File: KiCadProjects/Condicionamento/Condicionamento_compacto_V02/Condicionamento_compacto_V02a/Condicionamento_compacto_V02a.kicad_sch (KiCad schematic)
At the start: 28 parts, among them J2 Canais, J3 Entrada, J6 In_1 select, J7 In_2 select, U1-buffer1 AD828AN, U2-gain1 AD828AN, U3-Cond-DIP1 AD828AN, U4-Cond-SMD1 AD8056ARZ, U4-DigPot2 X9c10x, U5-DigPot1 X9c10x, U5-buffer1 AD8056ARZ, U6-gain1 AD8056ARZ

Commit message: agc
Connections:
- net GND is gone; now on net Earth: J3.6 (Pin_6), U4-DigPot2.2 (GND), U4-DigPot2.6 (GND), U5-DigPot1.2 (GND), U5-DigPot1.6 (GND)
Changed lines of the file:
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@@
+    (stroke (width 0) (type default))
+  )
+  (wire (pts (xy 234.95 148.59) (xy 238.76 148.59))
     (stroke (width 0) (type default))
   )
@@
         (path "/ca05a78d-0094-4531-91c3-e609c3923191"
           (reference "C4") (unit 1)
+        )
+      )
+    )
+  )
+  (symbol (lib_id "power:GND") (at 238.76 148.59 0) (mirror y) (unit 1)
+    (in_bom yes) (on_board yes) (dnp no) (fields_autoplaced)
+    (property "Reference" "#PWR028" (at 238.76 154.94 0)
+      (effects (font (size 1.27 1.27)) hide)
+    )
+    (property "Value" "Earth" (at 238.76 152.4 0)
+      (effects (font (size 1.27 1.27)) hide)
+    )
+    (property "Footprint" "" (at 238.76 148.59 0)
+      (effects (font (size 1.27 1.27)) hide)
+    )
+    (property "Datasheet" "~" (at 238.76 148.59 0)
+      (effects (font (size 1.27 1.27)) hide)
+    )
+    (pin "1")
+    (instances
+      (project "Condicionamento_compacto_V02a"
+        (path "/ca05a78d-0094-4531-91c3-e609c3923191"
+          (reference "#PWR028") (unit 1)
         )
       )
@@
         )
       )
+    )
+  )
+  (symbol (lib_id "power:Earth") (at 234.95 148.59 0) (mirror y) (unit 1)
+    (in_bom yes) (on_board yes) (dnp no) (fields_autoplaced)
+    (property "Reference" "#PWR027" (at 234.95 154.94 0)
+      (effects (font (size 1.27 1.27)) hide)
+    )
+    (property "Value" "Earth" (at 234.95 152.4 0)
+      (effects (font (size 1.27 1.27)) hide)
+    )
+    (property "Footprint" "" (at 234.95 148.59 0)
+      (effects (font (size 1.27 1.27)) hide)
+    )
+    (property "Datasheet" "~" (at 234.95 148.59 0)
+      (effects (font (size 1.27 1.27)) hide)
+    )
+    (pin "1")
+    (instances
+      (project "Condicionamento_compacto_V02a"
+        (path "/ca05a78d-0094-4531-91c3-e609c3923191"
+          (reference "#PWR027") (unit 1)
+        )
+      )

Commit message: tmp
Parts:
- added Cf1, Cf2: C, symbol Device:C
- added J1: jumper cf1, symbol Connector_Generic:Conn_01x02
- added J4: jumper cf2, symbol Connector_Generic:Conn_01x02
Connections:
- net Earth: now also Cf1.2, Cf2.2
- net auxiliar_1: now also J1.2 (Pin_2)
- net auxiliar_2: now also J4.2 (Pin_2)
- new net: Cf1.1, J1.1 (Pin_1)
- new net: Cf2.1, J4.1 (Pin_1)
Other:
- moved on the sheet: J6, J7, R10, R11, U2-gain1, U4-DigPot2, U5-DigPot1

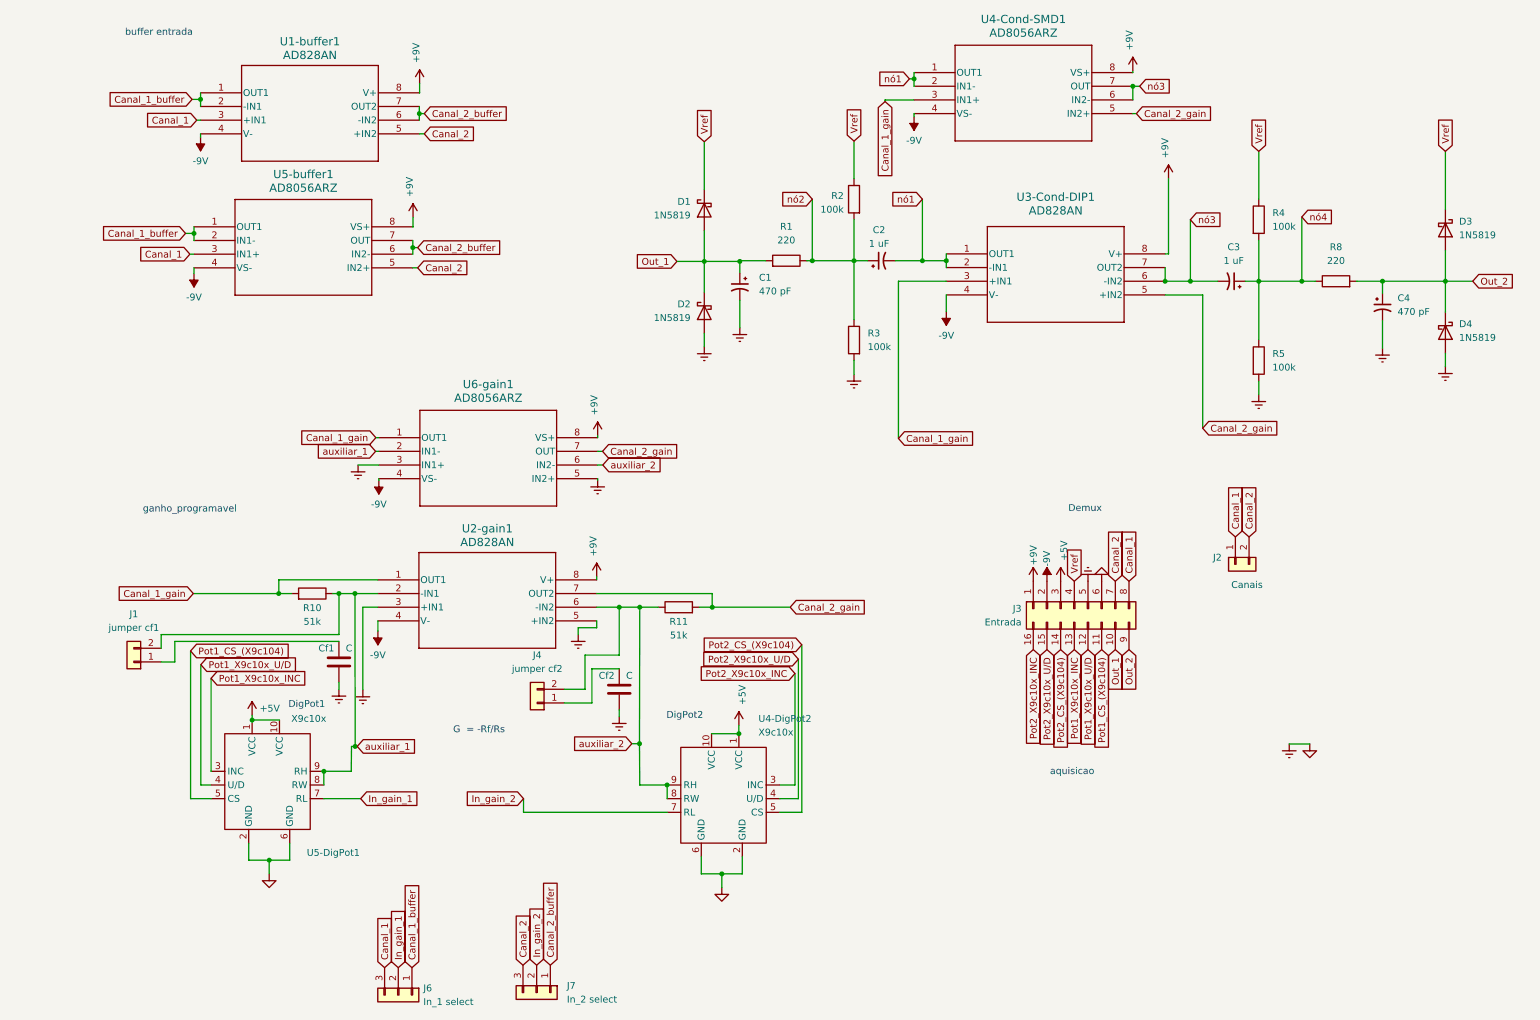
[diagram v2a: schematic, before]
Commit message: biblioteca analise sinal pelo osciloscopio
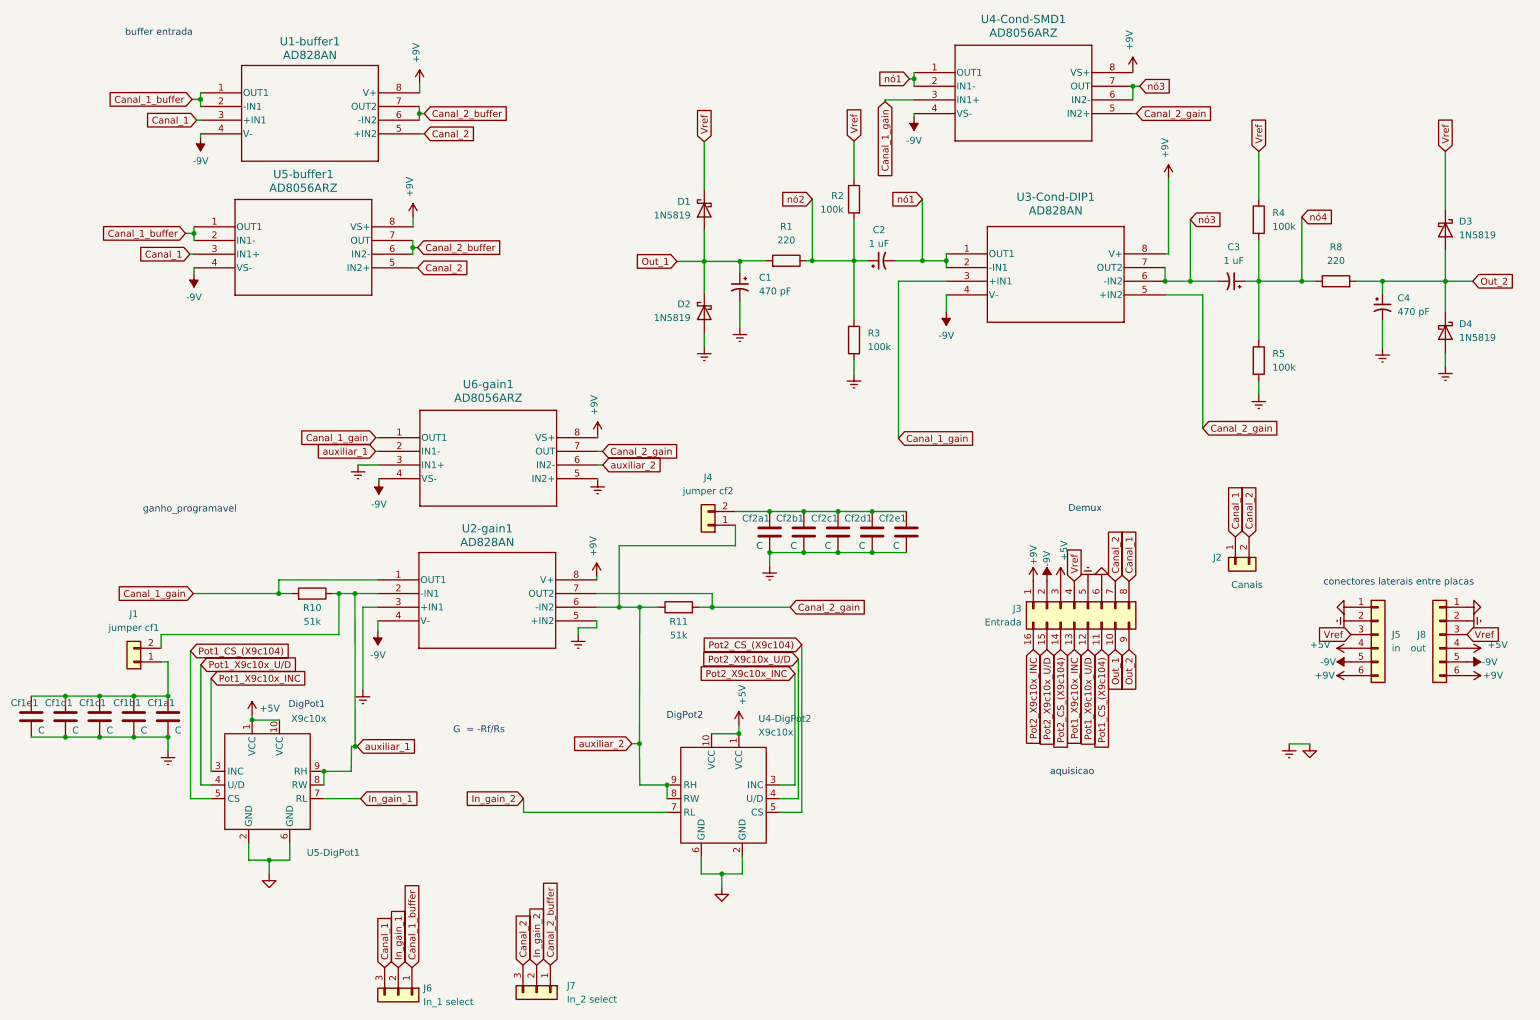
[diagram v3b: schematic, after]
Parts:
- removed Cf2: C, symbol Device:C
- added Cf1b1, Cf1c1, Cf1d1, Cf1e1, Cf2a1, Cf2b1, Cf2c1, Cf2d1, Cf2e1: C, Capacitor_THT:CP_Radial_D5.0mm_P2.50mm, symbol Device:C
- added J5: in, Connector_PinSocket_2.54mm:PinSocket_1x06_P2.54mm_Horizontal, symbol Connector_Generic:Conn_01x06
- added J8: out, Connector_PinHeader_2.54mm:PinHeader_1x06_P2.54mm_Horizontal, symbol Connector_Generic:Conn_01x06
- Cf1a1: renamed from Cf1; footprint (none) -> Capacitor_THT:CP_Radial_D5.0mm_P2.50mm
- J1: footprint (none) -> Connector_PinHeader_2.54mm:PinHeader_1x02_P2.54mm_Vertical
- J4: footprint (none) -> Connector_PinHeader_2.54mm:PinHeader_1x06_P2.54mm_Horizontal
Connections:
- net +5V: now also J5.4 (Pin_4), J8.4 (Pin_4)
- net +9V: now also J5.6 (Pin_6), J8.6 (Pin_6)
- net -9V: now also J5.5 (Pin_5), J8.5 (Pin_5)
- net Earth: now also Cf1b1.2, Cf1c1.2, Cf1d1.2, Cf1e1.2, Cf2a1.2, Cf2b1.2, Cf2c1.2, Cf2d1.2, Cf2e1.2, J5.1 (Pin_1), J5.2 (Pin_2), J8.1 (Pin_1), J8.2 (Pin_2)
- net Vref: now also J5.3 (Pin_3), J8.3 (Pin_3)
- net auxiliar_2: now also J4.1 (Pin_1); no longer J4.2 (Pin_2)
- net at Cf1a1.1, J1.1 (Pin_1): now also Cf1b1.1, Cf1c1.1, Cf1d1.1, Cf1e1.1
- new net: Cf2a1.1, Cf2b1.1, Cf2c1.1, Cf2d1.1, Cf2e1.1, J4.2 (Pin_2)
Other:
- note added: "conectores laterais entre placas"
- moved on the sheet: Cf1a1, J4

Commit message: versao digpot
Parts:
- removed Cf1c1, Cf1d1, Cf1e1, Cf2c1, Cf2d1, Cf2e1: C, Capacitor_THT:CP_Radial_D5.0mm_P2.50mm, symbol Device:C
- Cf2-select2: renamed from J4; footprint Connector_PinHeader_2.54mm:PinHeader_1x06_P2.54mm_Horizontal -> Connector_PinHeader_2.54mm:PinHeader_1x02_P2.54mm_Vertical
- renumbered J1 to Cf1-select1, J5 to J4, J8 to J5, J2 to J6, J6 to J7, J7 to J8
